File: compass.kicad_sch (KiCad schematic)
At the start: 8 parts, among them U1201 LIS3MDL

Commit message: (pcb) route SWD conn
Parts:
- C2: footprint Capacitor_SMD:C_0603_1608Metric -> Capacitor_SMD:C_0402_1005Metric
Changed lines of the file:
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@@
       (effects (font (size 1.27 1.27)) (justify left))
     )
-    (property "Footprint" "Capacitor_SMD:C_0603_1608Metric" (at 172.72 78.105 0)
+    (property "Footprint" "Capacitor_SMD:C_0402_1005Metric" (at 172.72 78.105 0)
       (effects (font (size 1.27 1.27)) hide)
     )

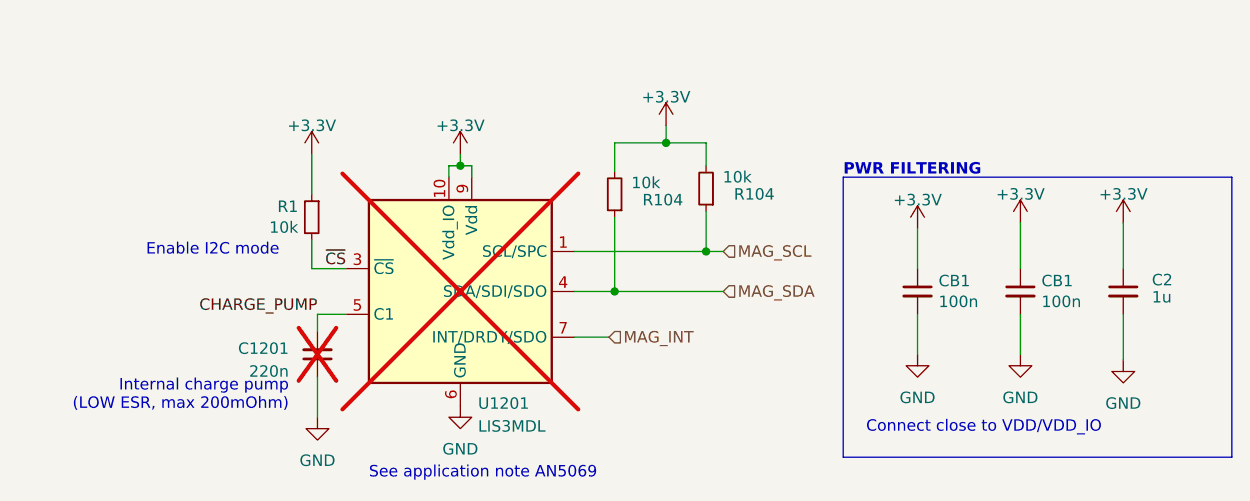
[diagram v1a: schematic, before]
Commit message: (pcb) route MAG & ENV sens.
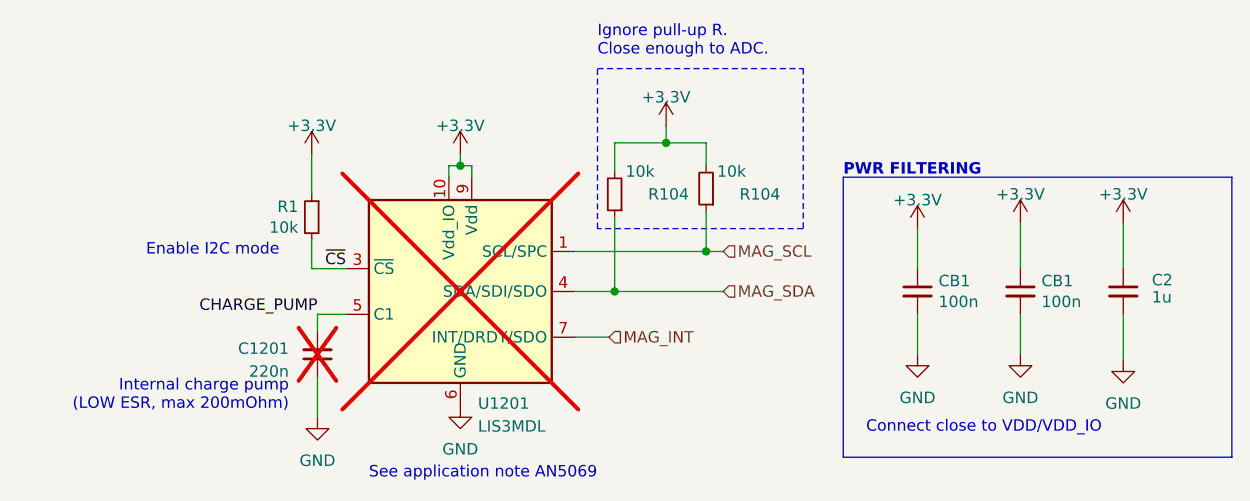
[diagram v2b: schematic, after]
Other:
- note added: "Ignore pull-up R. Close enough to ADC."
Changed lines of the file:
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@@
     (stroke (width 0) (type default))
+  )
+  (rectangle (start 114.3 53.34) (end 137.16 71.12)
+    (stroke (width 0) (type dash))
+    (fill (type none))
   )
   (rectangle (start 141.605 65.405) (end 184.785 96.52)
@@
     (effects (font (size 1.27 1.27)) (justify left bottom))
   )
+  (text "Ignore pull-up R. \nClose enough to ADC." (at 114.3 52.07 0)
+    (effects (font (size 1.27 1.27)) (justify left bottom))
+  )
   (text "Connect close to VDD/VDD_IO" (at 144.145 93.98 0)
     (effects (font (size 1.27 1.27)) (justify left bottom))
@@
   (symbol (lib_id "Device:R_Small") (at 116.205 67.31 180) (unit 1)
     (in_bom yes) (on_board yes) (dnp no)
-    (property "Reference" "R104" (at 123.825 67.945 0)
-      (effects (font (size 1.27 1.27)) (justify left))
-    )
-    (property "Value" "10k" (at 121.285 66.04 0)
+    (property "Reference" "R104" (at 124.46 67.31 0)
+      (effects (font (size 1.27 1.27)) (justify left))
+    )
+    (property "Value" "10k" (at 120.65 64.77 0)
       (effects (font (size 1.27 1.27)) (justify left))
     )
@@
         )
         (path "/4185c36c-c66e-4dbd-be5d-841e551f4885/3579cd31-f7d1-4b38-82cc-1314e00d3f8a"
-          (reference "R1203") (unit 1)
+          (reference "#R1203") (unit 1)
         )
       )
@@
   (symbol (lib_id "Device:R_Small") (at 126.365 66.675 180) (unit 1)
     (in_bom yes) (on_board yes) (dnp no)
-    (property "Reference" "R104" (at 133.985 67.31 0)
-      (effects (font (size 1.27 1.27)) (justify left))
-    )
-    (property "Value" "10k" (at 131.445 65.405 0)
+    (property "Reference" "R104" (at 134.62 67.31 0)
+      (effects (font (size 1.27 1.27)) (justify left))
+    )
+    (property "Value" "10k" (at 130.81 64.77 0)
       (effects (font (size 1.27 1.27)) (justify left))
     )
@@
         )
         (path "/4185c36c-c66e-4dbd-be5d-841e551f4885/3579cd31-f7d1-4b38-82cc-1314e00d3f8a"
-          (reference "R1202") (unit 1)
-        )
-      )
+          (reference "#R1202") (unit 1)
+        )
+      )

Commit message: (sch) fix +3.3V to 3v3 mislabel
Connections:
- net +3.3V renamed +3V3

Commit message: (sch) consoldate BOM
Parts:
- C2: MPN (none) -> C0402C105K9PACTU
- U1201: MPN DNP -> LIS3MDLTR; Mfr. DNP -> STMicroelectronics
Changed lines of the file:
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@@
       (effects (font (size 1.27 1.27)) hide)
     )
-    (property "MPN" "DNP" (at 99.06 78.105 0)
+    (property "MPN" "LIS3MDLTR" (at 99.06 78.105 0)
       (effects (font (size 1.27 1.27)) hide)
     )
-    (property "Mfr." "DNP" (at 99.06 78.105 0)
+    (property "Mfr." "STMicroelectronics" (at 99.06 78.105 0)
       (effects (font (size 1.27 1.27)) hide)
     )
@@
       (effects (font (size 1.27 1.27)) hide)
     )
-    (property "MPN" "" (at 172.72 78.105 0)
+    (property "MPN" "C0402C105K9PACTU" (at 172.72 78.105 0)
       (effects (font (size 1.27 1.27)) hide)
     )

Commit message: (sch) fix connector naming
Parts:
- C1201: MPN (none) -> GRT155R71A224KE01D; Mfr. (none) -> Murata
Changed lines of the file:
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@@
+      (effects (font (size 1.27 1.27)) hide)
+    )
+    (property "MPN" "GRT155R71A224KE01D" (at 83.185 85.09 0)
+      (effects (font (size 1.27 1.27)) hide)
+    )
+    (property "Mfr." "Murata" (at 83.185 85.09 0)
       (effects (font (size 1.27 1.27)) hide)
     )

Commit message: (sch) clean up items for BOM
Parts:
- C1201: now fitted
- U1201: now fitted; now in the parts list
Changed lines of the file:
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@@
   )
   (symbol (lib_id "grootvoet:LIS2MDL") (at 99.06 78.105 0) (unit 1)
-    (in_bom no) (on_board yes) (dnp yes) (fields_autoplaced)
+    (in_bom yes) (on_board yes) (dnp no) (fields_autoplaced)
     (property "Reference" "U1201" (at 101.0159 90.551 0)
       (effects (font (size 1.27 1.27)) (justify left))
@@
   )
   (symbol (lib_id "Device:C_Small") (at 83.185 85.09 0) (mirror x) (unit 1)
-    (in_bom yes) (on_board yes) (dnp yes)
+    (in_bom yes) (on_board yes) (dnp no)
     (property "Reference" "C1201" (at 80.01 84.4486 0)
       (effects (font (size 1.27 1.27)) (justify right))

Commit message: (pcb) update compass for manufacturing
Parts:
- U1201: footprint Package_LGA:LGA-12_2x2mm_P0.5mm -> grootvoet:LIS3MDL_LGA-12_2x2mm_P0.5mm
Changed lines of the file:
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@@
       (effects (font (size 1.27 1.27)) (justify left))
     )
-    (property "Footprint" "Package_LGA:LGA-12_2x2mm_P0.5mm" (at 129.54 85.725 0)
+    (property "Footprint" "grootvoet:LIS3MDL_LGA-12_2x2mm_P0.5mm" (at 129.54 85.725 0)
       (effects (font (size 1.27 1.27)) hide)
     )

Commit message: chore: update kicad version
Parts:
- renumbered R104 to #R1202, R104 to #R1203, C2 to C1202, CB1 to CB1201, CB1 to CB1202, R1 to R1201
